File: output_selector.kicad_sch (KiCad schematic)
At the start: 25 parts, among them J2 AVR-ISP-6, J3 PJ-393-8P, J4 PJ-603, K1 IM03DGR, Q2 BC817, U2 ATTINY9-TS8R

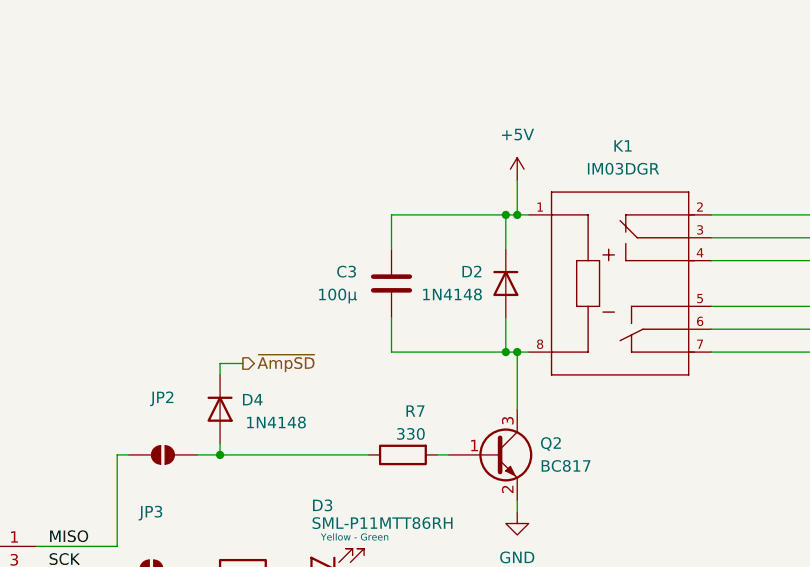
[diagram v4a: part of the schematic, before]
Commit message: source component and fix some lib
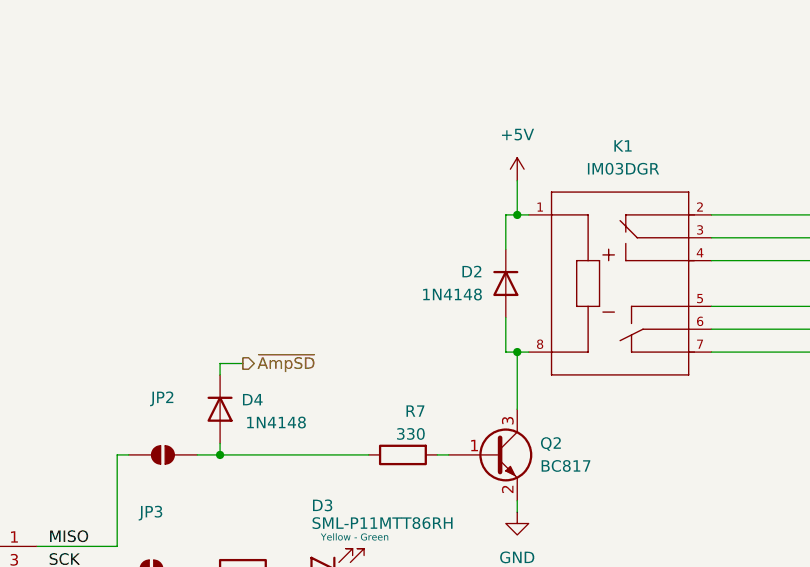
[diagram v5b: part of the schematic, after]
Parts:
- removed C3: 100µ, symbol Device:C
- C2: footprint (none) -> Capacitor_SMD:C_0402_1005Metric; LCSC Part (none) -> C77020
- D2, D4: footprint Diode_THT:D_DO-35_SOD27_P7.62mm_Horizontal -> Diode_SMD:D_SOD-123; LCSC Part (none) -> C5805632
- D3: LCSC Part (none) -> C2898986
- J2: footprint (none) -> Connector_PinSocket_2.54mm:PinSocket_1x06_P2.54mm_Vertical
- K1: LCSC Part (none) -> C5439567
- Q2: LCSC Part (none) -> C52801
- R10, R11, R12, R9: footprint (none) -> Resistor_SMD:R_0402_1005Metric; LCSC Part (none) -> C427211
- R6: footprint (none) -> Resistor_SMD:R_0402_1005Metric; LCSC Part (none) -> C427256
- R7: footprint (none) -> Resistor_SMD:R_0402_1005Metric; LCSC Part (none) -> C427206
- R8: footprint (none) -> Resistor_SMD:R_0402_1005Metric; LCSC Part (none) -> C413067
- S1: LCSC Part (none) -> C41430893
- U2: LCSC Part (none) -> C2052946
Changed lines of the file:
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@@
 	)
 	(junction
-		(at 218.44 119.38)
-		(diameter 0)
-		(color 0 0 0 0)
-	)
-	(junction
 		(at 219.71 119.38)
 		(diameter 0)
@@
 	)
 	(junction
-		(at 218.44 134.62)
-		(diameter 0)
-		(color 0 0 0 0)
-	)
-	(junction
 		(at 262.89 135.89)
 		(diameter 0)
@@
 	(wire
 		(pts
-			(xy 205.74 123.19) (xy 205.74 119.38)
-		)
-		(stroke
-			(width 0)
-			(type default)
-		)
-	)
-	(wire
-		(pts
 			(xy 241.3 119.38) (xy 259.08 119.38)
 		)
@@
 	(wire
 		(pts
-			(xy 205.74 119.38) (xy 218.44 119.38)
-		)
-		(stroke
-			(width 0)
-			(type default)
-		)
-	)
-	(wire
-		(pts
 			(xy 66.04 154.94) (xy 66.04 156.21)
 		)
@@
 	(wire
 		(pts
-			(xy 205.74 134.62) (xy 218.44 134.62)
-		)
-		(stroke
-			(width 0)
-			(type default)
-		)
-	)
-	(wire
-		(pts
 			(xy 175.26 146.05) (xy 175.26 156.21)
 		)
@@
 	(wire
 		(pts
-			(xy 205.74 130.81) (xy 205.74 134.62)
-		)
-		(stroke
-			(width 0)
-			(type default)
-		)
-	)
-	(wire
-		(pts
 			(xy 262.89 135.89) (xy 264.16 135.89)
 		)
@@
 			)
 		)
-		(property "Footprint" ""
+		(property "Footprint" "Capacitor_SMD:C_0402_1005Metric"
 			(at 120.9548 163.83 0)
 			(effects
@@
 			)
 		)
+		(property "LCSC Part" "C77020"
+			(at 121.92 167.64 0)
+			(effects
+				(font
+					(size 1.27 1.27)
+				)
+				(hide yes)
+			)
+		)
 		(pin "2"
 		)
@@
 	)
 	(symbol
-		(lib_id "Device:C")
-		(at 205.74 127 0)
-		(mirror x)
-		(unit 1)
-		(exclude_from_sim no)
-		(in_bom yes)
-		(on_board yes)
-		(dnp no)
-		(property "Reference" "C3"
-			(at 201.93 125.7299 0)
-			(effects
-				(font
-					(size 1.27 1.27)
-				)
-				(justify right)
-			)
-		)
-		(property "Value" "100µ"
-			(at 201.93 128.2699 0)
-			(effects
-				(font
-					(size 1.27 1.27)
-				)
-				(justify right)
-			)
-		)
-		(property "Footprint" ""
-			(at 206.7052 123.19 0)
-			(effects
-				(font
-					(size 1.27 1.27)
-				)
-				(hide yes)
-			)
-		)
-		(property "Datasheet" "~"
-			(at 205.74 127 0)
-			(effects
-				(font
-					(size 1.27 1.27)
-				)
-				(hide yes)
-			)
-		)
-		(property "Description" "Unpolarized capacitor"
-			(at 205.74 127 0)
-			(effects
-				(font
-					(size 1.27 1.27)
-				)
-				(hide yes)
-			)
-		)
-		(pin "2"
-		)
-		(pin "1"
-		)
-		(instances
-			(project "AudioInterface"
-				(path "/0650c7a8-acba-429c-9f8e-eec0baf0bc1c/fede4c36-00cc-4d3d-b71c-5243ba232202/86fedcf6-4284-4ef9-aa8f-0fb0258e957c"
-					(reference "C3")
-					(unit 1)
-				)
-			)
-		)
-	)
-	(symbol
 		(lib_id "0 __:ATTINY9-TS8R")
 		(at 166.37 156.21 0)
@@
 			)
 		)
+		(property "LCSC Part" "C2052946"
+			(at 166.37 156.21 0)
+			(effects
+				(font
+					(size 1.27 1.27)
+				)
+				(hide yes)
+			)
+		)
 		(pin "3"
 		)
@@
 			)
 		)
-		(property "Footprint" "Diode_THT:D_DO-35_SOD27_P7.62mm_Horizontal"
+		(property "Footprint" "Diode_SMD:D_SOD-123"
 			(at 186.69 140.97 0)
 			(effects
@@
 			)
 		)
+		(property "LCSC Part" " C5805632"
+			(at 186.69 140.97 0)
+			(effects
+				(font
+					(size 1.27 1.27)
+				)
+				(hide yes)
+			)
+		)
 		(pin "1"
 		)
@@
 			)
 		)
-		(property "Footprint" ""
+		(property "Footprint" "Resistor_SMD:R_0402_1005Metric"
 			(at 86.36 115.062 90)
 			(effects
@@
 			)
 		)
+		(property "LCSC Part" "C427211"
+			(at 86.36 116.84 0)
+			(effects
+				(font
+					(size 1.27 1.27)
+				)
+				(hide yes)
+			)
+		)
 		(pin "1"
 		)
@@
 			)
 		)
-		(property "Footprint" "Diode_THT:D_DO-35_SOD27_P7.62mm_Horizontal"
+		(property "Footprint" "Diode_SMD:D_SOD-123"
 			(at 218.44 127 0)
 			(effects
@@
 			)
 		)
+		(property "LCSC Part" " C5805632"
+			(at 218.44 127 0)
+			(effects
+				(font
+					(size 1.27 1.27)
+				)
+				(hide yes)
+			)
+		)
 		(pin "1"
 		)
@@
 			)
 		)
-		(property "Footprint" ""
+		(property "Footprint" "Resistor_SMD:R_0402_1005Metric"
 			(at 189.23 160.528 90)
 			(effects
@@
 			)
 		)
+		(property "LCSC Part" "C413067"
+			(at 189.23 158.75 0)
+			(effects
+				(font
+					(size 1.27 1.27)
+				)
+				(hide yes)
+			)
+		)
 		(pin "1"
 		)
@@
 			)
 		)
+		(property "LCSC Part" " C52801"
+			(at 217.17 146.05 0)
+			(effects
+				(font
+					(size 1.27 1.27)
+				)
+				(hide yes)
+			)
+		)
 		(pin "2"
 		)
@@
 			)
 		)
+		(property "LCSC Part" "C5439567"
+			(at 231.14 127 0)
+			(effects
+				(font
+					(size 1.27 1.27)
+				)
+				(hide yes)
+			)
+		)
 		(pin "3"
 		)
@@
 			)
 		)
-		(property "Footprint" ""
+		(property "Footprint" "Resistor_SMD:R_0402_1005Metric"
 			(at 110.998 151.13 90)
 			(effects
@@
 			)
 		)
+		(property "LCSC Part" "C427256"
+			(at 109.22 151.13 0)
+			(effects
+				(font
+					(size 1.27 1.27)
+				)
+				(hide yes)
+			)
+		)
 		(pin "1"
 		)
@@
 			)
 		)
-		(property "Footprint" ""
+		(property "Footprint" "Resistor_SMD:R_0402_1005Metric"
 			(at 86.36 117.602 90)
 			(effects
@@
 			)
 		)
+		(property "LCSC Part" "C427211"
+			(at 86.36 119.38 0)
+			(effects
+				(font
+					(size 1.27 1.27)
+				)
+				(hide yes)
+			)
+		)
 		(pin "1"
 		)
@@
 			)
 		)
-		(property "Footprint" ""
+		(property "Footprint" "Resistor_SMD:R_0402_1005Metric"
 			(at 207.01 144.272 90)
 			(effects
@@
 			)
 		)
+		(property "LCSC Part" "C427206"
+			(at 207.01 146.05 0)
+			(effects
+				(font
+					(size 1.27 1.27)
+				)
+				(hide yes)
+			)
+		)
 		(pin "1"
 		)
@@
 			)
 		)
-		(property "Footprint" ""
+		(property "Footprint" "Resistor_SMD:R_0402_1005Metric"
 			(at 86.36 120.142 90)
 			(effects
@@
 			)
 		)
+		(property "LCSC Part" "C427211"
+			(at 86.36 121.92 0)
+			(effects
+				(font
+					(size 1.27 1.27)
+				)
+				(hide yes)
+			)
+		)
 		(pin "1"
 		)
@@
 			)
 		)
+		(property "LCSC Part" "C2898986"
+			(at 198.12 158.75 0)
+			(effects
+				(font
+					(size 1.27 1.27)
+				)
+				(hide yes)
+			)
+		)
 		(pin "2"
 		)
@@
 			)
 		)
+		(property "LCSC Part" "C41430893"
+			(at 115.57 161.29 0)
+			(effects
+				(font
+					(size 1.27 1.27)
+				)
+				(hide yes)
+			)
+		)
 		(pin "1"
 		)
@@
 			)
 		)
-		(property "Footprint" ""
+		(property "Footprint" "Resistor_SMD:R_0402_1005Metric"
 			(at 86.36 112.522 90)
 			(effects
@@
 			)
 		)
+		(property "LCSC Part" "C427211"
+			(at 86.36 114.3 0)
+			(effects
+				(font
+					(size 1.27 1.27)
+				)
+				(hide yes)
+			)
+		)
 		(pin "1"
 		)
@@
 			)
 		)
-		(property "Footprint" ""
+		(property "Footprint" "Connector_PinSocket_2.54mm:PinSocket_1x06_P2.54mm_Vertical"
 			(at 64.77 118.11 90)
 			(effects

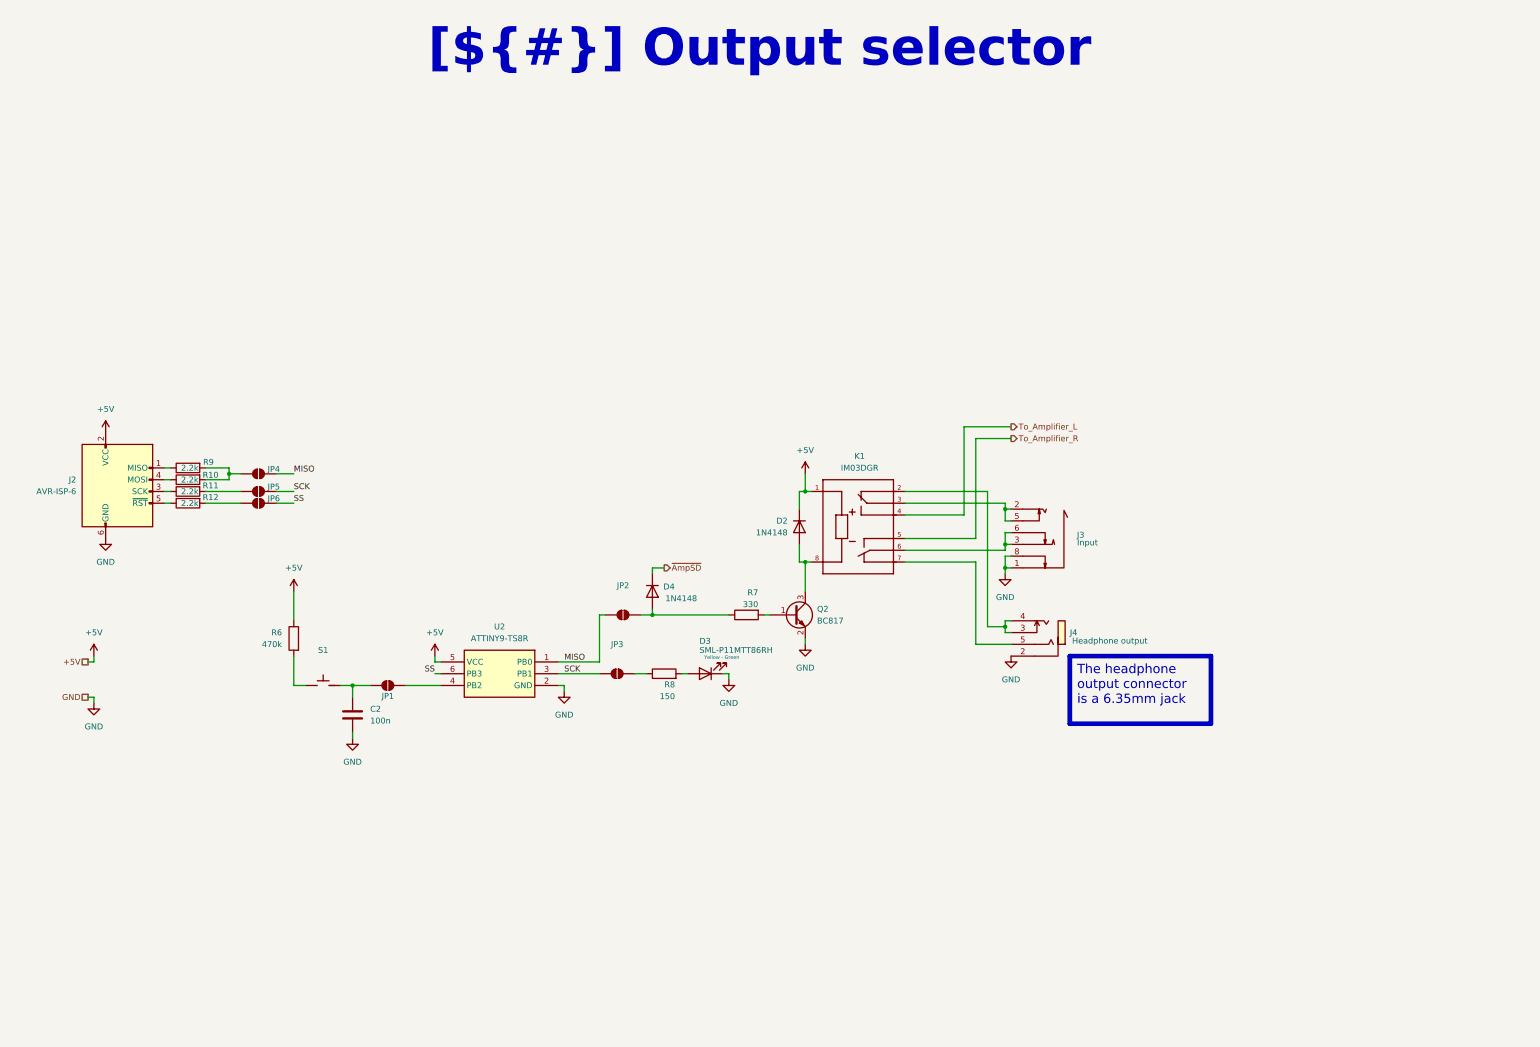
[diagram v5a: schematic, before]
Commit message: add connector to separate the selector switch and led indicator
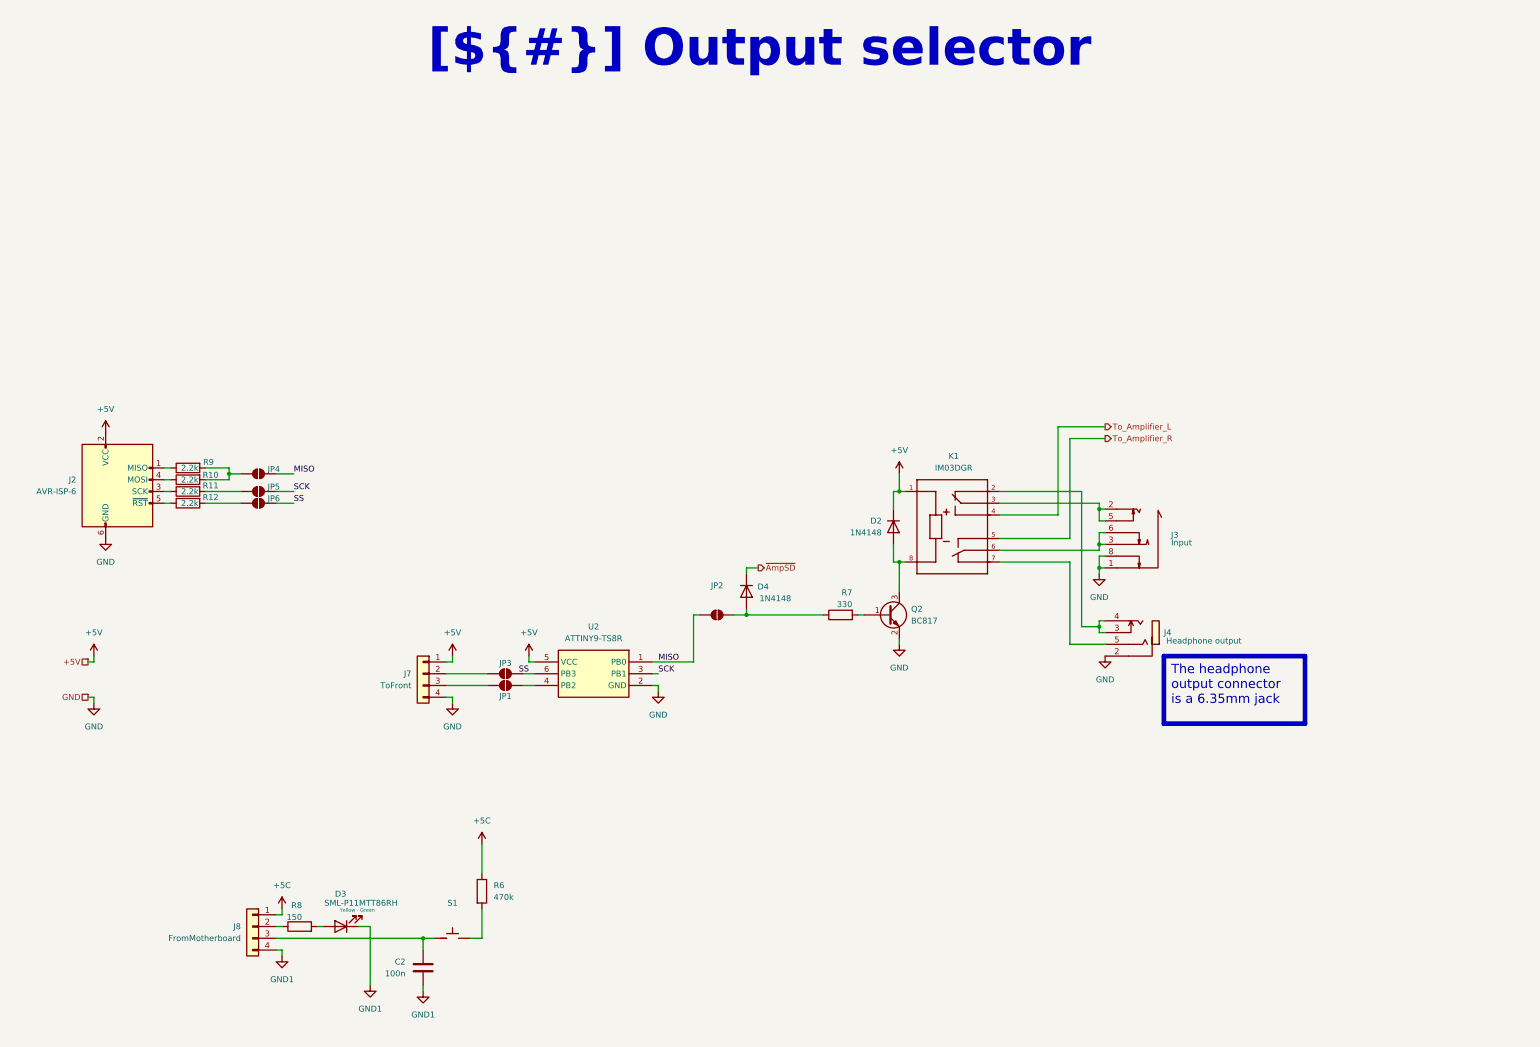
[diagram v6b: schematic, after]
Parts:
- added J7: ToFront, Connector_PinHeader_2.54mm:PinHeader_1x04_P2.54mm_Vertical, symbol Connector_Generic:Conn_01x04
- added J8: FromMotherboard, Connector_PinHeader_2.54mm:PinHeader_1x04_P2.54mm_Vertical, symbol Connector_Generic:Conn_01x04
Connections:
- net +5V: now also J7.1 (Pin_1); no longer R6.1
- net GND: now also J7.4 (Pin_4); no longer C2.1, D3.1 (K)
- net SCK: no longer JP3.1 (A)
- net SS: now also JP3.1 (A)
- net at C2.2, S1.2: now also J8.3 (Pin_3); no longer JP1.1 (A)
- net at JP3.2 (B): now also J7.2 (Pin_2); no longer R8.1
- new net: J7.3 (Pin_3), JP1.1 (A)
- new net: J8.2 (Pin_2), R8.1
- new net +5C: J8.1 (Pin_1), R6.1
- new net GND1: C2.1, D3.1 (K), J8.4 (Pin_4)
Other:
- moved on the sheet: D2, D4, J3, J4, JP1, JP2, K1, Q2, R7, U2

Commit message: finish pcb and generate production file
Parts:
- added H5, H6: MountingHole_Pad, MountingHole:MountingHole_3.2mm_M3_Pad_Via, symbol Mechanical:MountingHole_Pad
- J2: footprint Connector_PinSocket_2.54mm:PinSocket_1x06_P2.54mm_Vertical -> Connector_PinSocket_2.54mm:PinSocket_2x03_P2.54mm_Vertical
- J7, J8: now left out of the parts list
- S1: footprint 0__:SW_PG151101S11 -> 0__:Kailh_socket_MX
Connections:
- net GND1: now also H5.1, H6.1
